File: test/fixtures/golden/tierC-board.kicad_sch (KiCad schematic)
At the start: 5 parts, among them J1 Conn_01x03, U1 MCU8

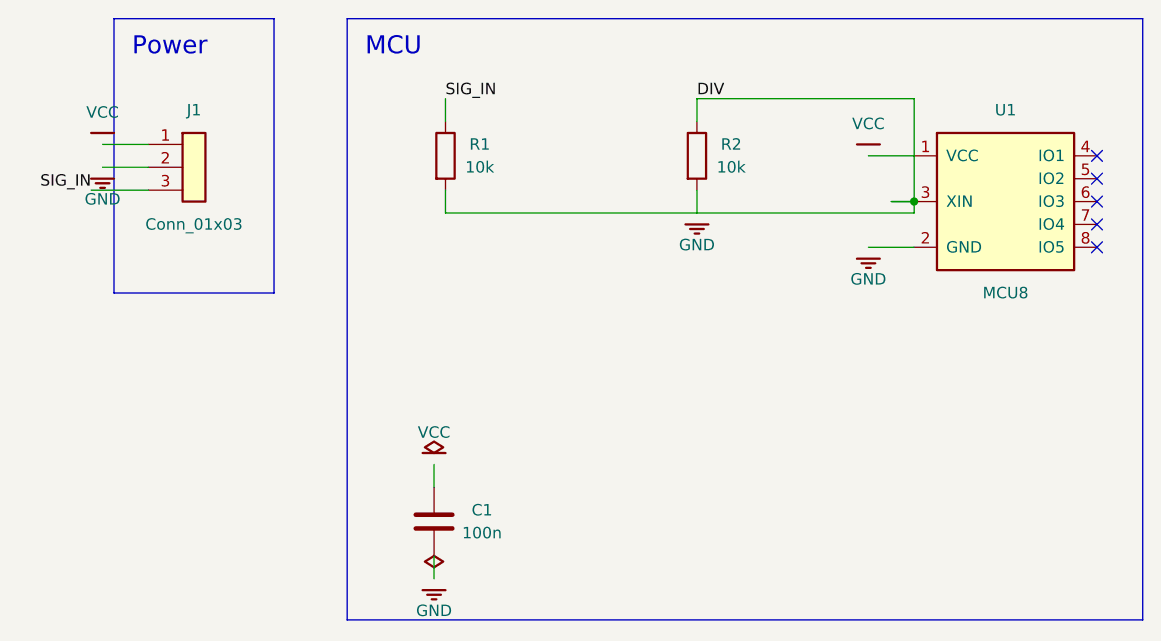
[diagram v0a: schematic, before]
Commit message: fix(draft): never route through a foreign connection point; gate wire-level net merges
Closes #204 (I22). The lemondrop run shipped a schematic whose crystal drive
was shorted onto TOUCH_IRQ: the trunk-and-branch router picks the median
stub-end x as its trunk, which for a net with pins on one symbol side IS the
stub/label column, and its only veto was wire-through-body. KiCad joins a
wire endpoint resting on another wire's interior, so the trunk down the
column of neighbouring stub ends merged nets, survived every intent-level
lever (rename, paper size, group order, declaration order), and ERC demoted
the merge to a warning.

Three layers:

- Router avoidance: a trunk-and-branch candidate is rejected when any of its
  segments touches a FOREIGN connection point — a pin, the stub end any
  connected pin grows (predicted, since labelled stubs of later nets are not
  emitted yet), or an already-emitted wire of another net. Falls through the
  remaining candidates to the labelled fallback, which cannot merge.

- Chain-pass hardening: axisClear additionally rejects a horizontal foreign
  stub SEGMENT crossing the axis exactly at a chain connection row of a
  different net (net-aware: ownEps is too coarse — U1's VCC pin shares a net
  with the chain's rail end, yet its stub through a SIG row still merges;
  moved parts are skipped since `placed` holds their stale positions). Chain
  drops retry with a bounded lift instead of parking a lead on an occupied
  row, so the pull-up idiom survives one grid row higher.

- Gate: findWireContactMerges detects cross-net wire contact (endpoint on a
  foreign wire, shared endpoints, a label anchored on a foreign net's wire)
  and feeds the existing merged-net refusal, so no future pass can ship the
  geometry silently — the label-position check alone cannot see any of this.

The pinned golden corpus contained the defect: tierC-board had DIV shorted to
GND at R2.2's stub end (its "clean" ERC was lib_symbol_issues noise), and the
pull-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
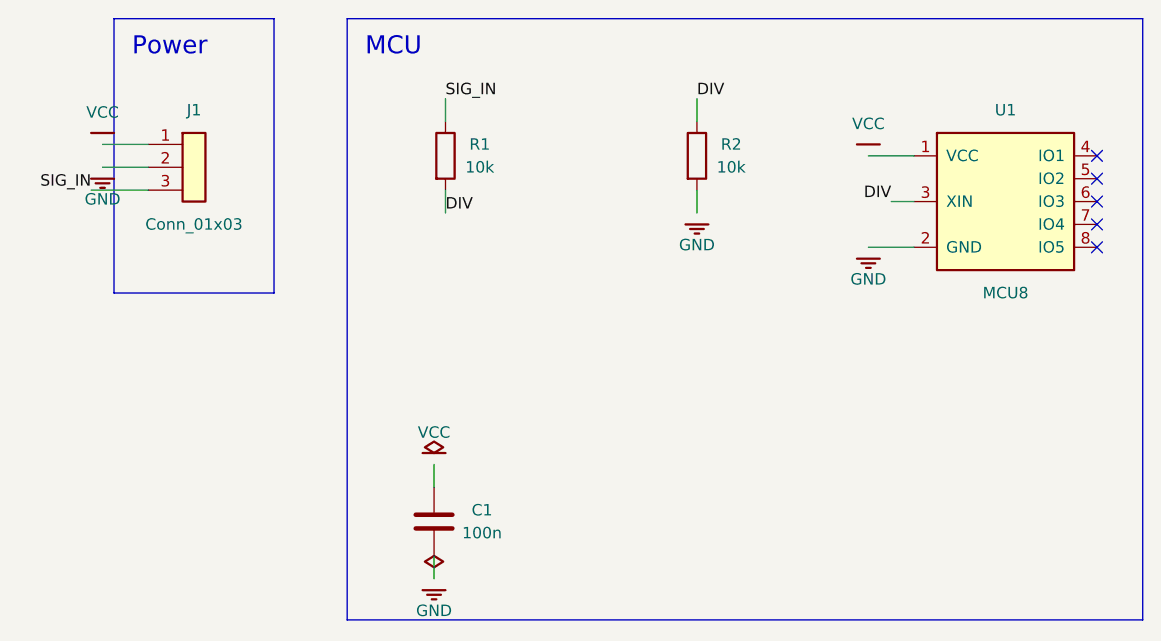
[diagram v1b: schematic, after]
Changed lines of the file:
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@@
 		(rev "A")
-	)
-	(junction (at 137.16 50.8)
-		(diameter 0)
-		(color 0 0 0 0)
 	)
 	(no_connect (at 157.48 45.72))
@@
 	)
 	(wire
-		(pts (xy 85.09 52.07) (xy 137.16 52.07))
-		(stroke (width 0) (type default))
-	)
-	(wire
 		(pts (xy 113.03 41.91) (xy 113.03 39.37))
 		(stroke (width 0) (type default))
 	)
 	(wire
-		(pts (xy 113.03 39.37) (xy 137.16 39.37))
-		(stroke (width 0) (type default))
-	)
-	(wire
 		(pts (xy 137.16 50.8) (xy 134.62 50.8))
-		(stroke (width 0) (type default))
-	)
-	(wire
-		(pts (xy 134.62 50.8) (xy 137.16 50.8))
-		(stroke (width 0) (type default))
-	)
-	(wire
-		(pts (xy 137.16 39.37) (xy 137.16 50.8))
-		(stroke (width 0) (type default))
-	)
-	(wire
-		(pts (xy 137.16 50.8) (xy 137.16 52.07))
 		(stroke (width 0) (type default))
 	)
@@
 		(effects (font (size 2 2)) (justify left top))
 	)
+	(label "DIV" (at 85.09 52.07 0)
+		(effects (font (size 1.27 1.27)) (justify left bottom))
+	)
 	(label "DIV" (at 113.03 39.37 0)
 		(effects (font (size 1.27 1.27)) (justify left bottom))
 	)
+	(label "DIV" (at 134.62 50.8 0)
+		(effects (font (size 1.27 1.27)) (justify right bottom))
+	)
 	(label "SIG_IN" (at 45.72 49.53 0)
